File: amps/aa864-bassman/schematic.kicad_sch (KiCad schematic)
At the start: 102 parts, among them T1 125P7D, T2 125C1A, T3 125A13A

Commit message: Fix: schematic sheets — real title block, fitted paper, no lettering through circuitry
Every sheet in the corpus shipped with an EMPTY title block ("Title:" and
"Date:" blank, default "Sheet /" furniture) laid onto a fixed A4/A3 page
regardless of the drawing's size, with prose annotations placed by hand
wherever a coordinate looked free when the amp was first drawn. The result
read as an unfinished alpha under a `verified` badge: KiCanvas's default view
is `zoom_to_page()`, so a 150 x 110 mm circuit on an A3 sheet opened as a
postage stamp, and later edits had pushed live circuitry under the prose.

schematic_lib.py — the builder now records each element as a (kind, points,
extra) tuple instead of a finished string, so `write()` can measure and move
what it emits:

- emits a real `(title_block …)` read from the amp's own meta.yaml — Title =
  designation + style, Date = the verification (or added) date, Rev = the
  verification status, Company = Circuit Codex, plus the licence and source
  URL as comments. Fixes all 34 sheets from one place;
- emits `(paper "User" w h)` cut to the drawing, translated to a fixed margin,
  with the bottom 34 mm strip reserved for the worksheet's title block. Sheet
  utilisation of the drawable area went from as low as ~20% to 92-98%;
- `note()` queues prose into a wrapped band under the circuit, and `caption()`
  places a section heading over the block it names, nudging it clear if it
  would print through anything;
- per-symbol default label offsets (the old single default printed every pot's
  value through its own wiper arrow and every transformer's designator through
  its body), plus `place_labels()`, which moves any designator/value block that
  would print over ink;
- transformers and chokes are drawn, not boxed: iron core between two windings,
  centre taps where the part has them, and an optional `spec` lettering slot for
  a ratio or impedance;
- `gnd()` takes a direction, because a flag defaulting to "down" at the HEAD of
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
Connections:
- net at D5.2 (K): no longer D6.1 (A)
- net at D3.1 (A): no longer D2.2 (K)
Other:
- note removed: "AA864 — Blackface Bassman-style · Circuit Codex · CC-BY-SA 4.0 · redrawn from circuit facts"
- company: (none) -> Circuit Codex
- title: (none) -> AA864 (Bassman) — Blackface Bassman-style

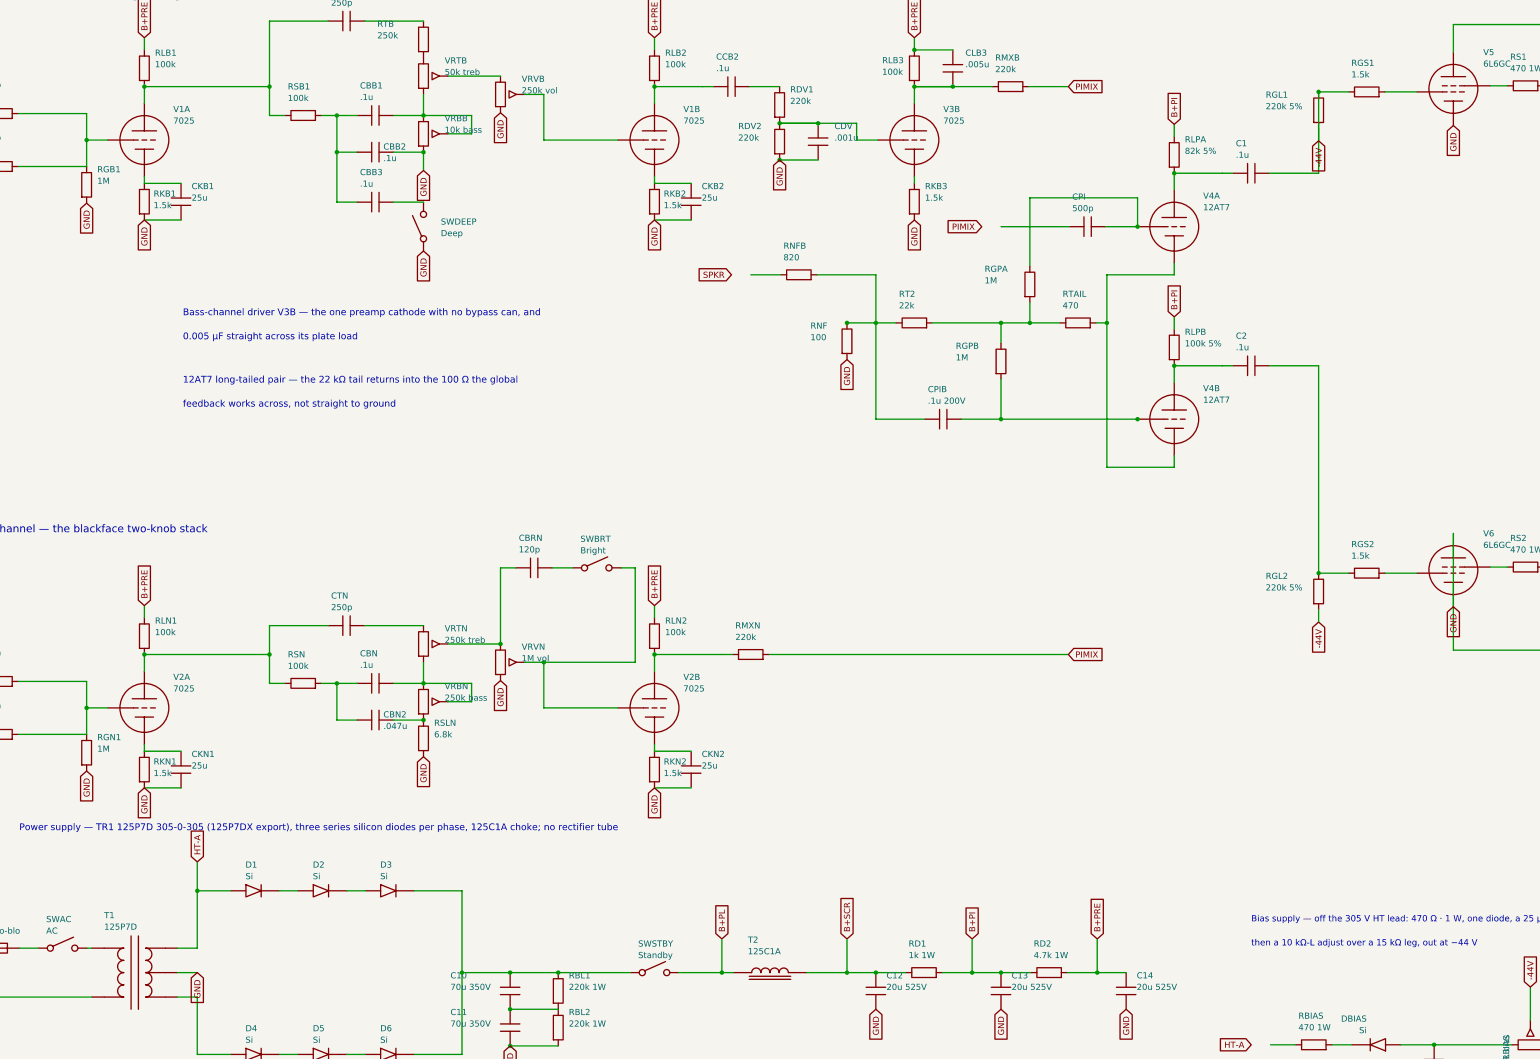
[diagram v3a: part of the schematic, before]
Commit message: Fix: deterministic schematic ids and wires split at every join
- _u() is uuid5 over (amp id, emission order), so a regeneration of an
  unchanged script is byte-identical and a drift gate becomes possible
- write() splits wire segments at symbol pins, wire ends and junction dots,
  so the file connects exactly what the drawing shows under KiCad's
  endpoint-only semantics (270 pins were on a wire's interior; net
  partitions unchanged on all 38 sheets)
- all sheets regenerated; aa864-bassman title block was stale (draft) and
  now matches meta.yaml (verified)

Co-Authored-By: Claude Fable 5.1 <noreply@anthropic.com>
Claude-Session: https://claude.ai/code/session_01KBMfdh37HmCL2iWcBiL5J1
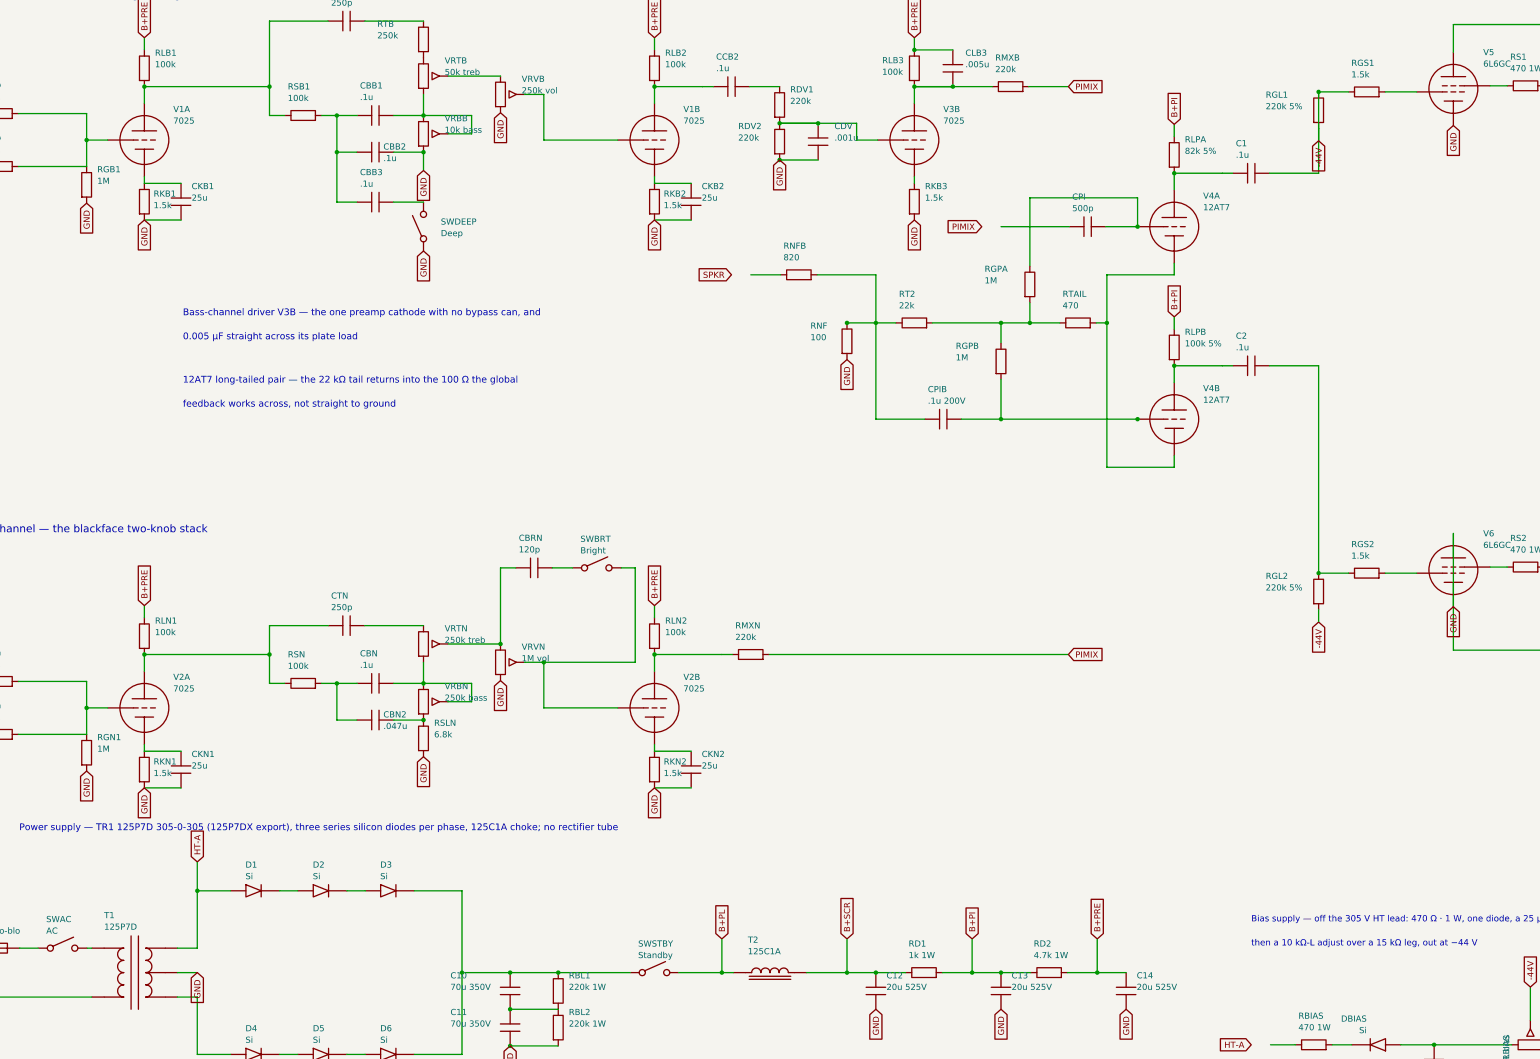
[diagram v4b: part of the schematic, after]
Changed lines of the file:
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@@
   (title_block
     (title "AA864 (Bassman) — Blackface Bassman-style")
-    (date "2026-08-08")
-    (rev "draft")
+    (date "2026-08-13")
+    (rev "verified")
     (company "Circuit Codex")
     (comment 1 "Redrawn from circuit facts — not a reproduction of any factory drawing")
@@
   (wire (pts (xy 36.2824 50.009) (xy 50.4724 50.009))
     (stroke (width 0) (type default)))
-  (wire (pts (xy 50.4724 39.009) (xy 50.4724 50.009))
+  (wire (pts (xy 50.4724 39.009) (xy 50.4724 44.509))
+    (stroke (width 0) (type default)))
+  (wire (pts (xy 50.4724 44.509) (xy 50.4724 50.009))
     (stroke (width 0) (type default)))
   (junction (at 50.4724 44.509) (diameter 0) (color 0 0 0 0))
@@
   (text "0.005 µF straight across its plate load" (at 70.4724 85.509 0)
     (effects (font (size 1.4 1.4)) (justify left)))
-  (wire (pts (xy 194.472 41.029) (xy 210.472 41.029))
+  (wire (pts (xy 194.472 41.029) (xy 202.472 41.029))
+    (stroke (width 0) (type default)))
+  (wire (pts (xy 202.472 41.029) (xy 210.472 41.029))
     (stroke (width 0) (type default)))
   (junction (at 202.472 41.029) (diameter 0) (color 0 0 0 0))
@@
   (global_label "GND" (shape input) (at 222.472 61.129 270)
     (effects (font (size 1.27 1.27)) (justify right)))
-  (wire (pts (xy 222.472 33.409) (xy 238.662 33.409))
+  (wire (pts (xy 222.472 33.409) (xy 230.472 33.409))
+    (stroke (width 0) (type default)))
+  (wire (pts (xy 230.472 33.409) (xy 238.662 33.409))
     (stroke (width 0) (type default)))
   (junction (at 230.472 33.409) (diameter 0) (color 0 0 0 0))
@@
   (wire (pts (xy 36.2824 168.009) (xy 50.4724 168.009))
     (stroke (width 0) (type default)))
-  (wire (pts (xy 50.4724 157.009) (xy 50.4724 168.009))
+  (wire (pts (xy 50.4724 157.009) (xy 50.4724 162.509))
+    (stroke (width 0) (type default)))
+  (wire (pts (xy 50.4724 162.509) (xy 50.4724 168.009))
     (stroke (width 0) (type default)))
   (junction (at 50.4724 162.509) (diameter 0) (color 0 0 0 0))
@@
   (wire (pts (xy 276.472 72.509) (xy 262.472 72.509))
     (stroke (width 0) (type default)))
-  (wire (pts (xy 262.472 72.509) (xy 262.472 112.509))
+  (wire (pts (xy 262.472 72.509) (xy 262.472 82.509))
+    (stroke (width 0) (type default)))
+  (wire (pts (xy 262.472 82.509) (xy 262.472 112.509))
     (stroke (width 0) (type default)))
   (wire (pts (xy 262.472 112.509) (xy 276.472 112.509))
@@
   (wire (pts (xy 262.472 82.509) (xy 260.282 82.509))
     (stroke (width 0) (type default)))
-  (wire (pts (xy 252.662 82.509) (xy 240.472 82.509))
+  (wire (pts (xy 252.662 82.509) (xy 246.472 82.509))
+    (stroke (width 0) (type default)))
+  (wire (pts (xy 246.472 82.509) (xy 240.472 82.509))
     (stroke (width 0) (type default)))
   (junction (at 246.472 82.509) (diameter 0) (color 0 0 0 0))
@@
     (property "Reference" "CPIB" (at 225.272 96.309 270) (effects (font (size 1.27 1.27)) (justify left)))
     (property "Value" ".1u 200V" (at 225.272 98.709 270) (effects (font (size 1.27 1.27)) (justify left))))
-  (wire (pts (xy 232.282 102.509) (xy 268.852 102.509))
+  (wire (pts (xy 232.282 102.509) (xy 240.472 102.509))
+    (stroke (width 0) (type default)))
+  (wire (pts (xy 240.472 102.509) (xy 268.852 102.509))
     (stroke (width 0) (type default)))
   (junction (at 268.852 102.509) (diameter 0) (color 0 0 0 0))
@@
   (wire (pts (xy 296.282 51.409) (xy 306.472 51.409))
     (stroke (width 0) (type default)))
-  (wire (pts (xy 306.472 51.409) (xy 306.472 34.509))
+  (wire (pts (xy 306.472 51.409) (xy 306.472 44.669))
+    (stroke (width 0) (type default)))
+  (wire (pts (xy 306.472 44.669) (xy 306.472 42.129))
+    (stroke (width 0) (type default)))
+  (wire (pts (xy 306.472 42.129) (xy 306.472 34.509))
     (stroke (width 0) (type default)))
   (wire (pts (xy 276.472 91.409) (xy 286.472 91.409))
@@
   (wire (pts (xy 366.472 79.429) (xy 373.582 79.429))
     (stroke (width 0) (type default)))
-  (wire (pts (xy 334.472 126.254) (xy 334.472 150.509))
+  (wire (pts (xy 334.472 126.254) (xy 334.472 141.494))
+    (stroke (width 0) (type default)))
+  (wire (pts (xy 334.472 141.494) (xy 334.472 150.509))
     (stroke (width 0) (type default)))
   (wire (pts (xy 334.472 150.509) (xy 362.472 150.509))
@@
   (wire (pts (xy 182.472 217.509) (xy 184.852 217.509))
     (stroke (width 0) (type default)))
-  (wire (pts (xy 200.092 217.509) (xy 214.472 217.509))
+  (wire (pts (xy 200.092 217.509) (xy 208.472 217.509))
+    (stroke (width 0) (type default)))
+  (wire (pts (xy 208.472 217.509) (xy 214.472 217.509))
     (stroke (width 0) (type default)))
   (junction (at 208.472 217.509) (diameter 0) (color 0 0 0 0))
@@
   (wire (pts (xy 214.472 217.509) (xy 220.662 217.509))
     (stroke (width 0) (type default)))
-  (wire (pts (xy 228.282 217.509) (xy 240.472 217.509))
+  (wire (pts (xy 228.282 217.509) (xy 234.472 217.509))
+    (stroke (width 0) (type default)))
+  (wire (pts (xy 234.472 217.509) (xy 240.472 217.509))
     (stroke (width 0) (type default)))
   (junction (at 234.472 217.509) (diameter 0) (color 0 0 0 0))
@@
   (wire (pts (xy 240.472 217.509) (xy 246.662 217.509))
     (stroke (width 0) (type default)))
-  (wire (pts (xy 254.282 217.509) (xy 266.472 217.509))
+  (wire (pts (xy 254.282 217.509) (xy 260.472 217.509))
+    (stroke (width 0) (type default)))
+  (wire (pts (xy 260.472 217.509) (xy 266.472 217.509))
     (stroke (width 0) (type default)))
   (junction (at 260.472 217.509) (diameter 0) (color 0 0 0 0))
